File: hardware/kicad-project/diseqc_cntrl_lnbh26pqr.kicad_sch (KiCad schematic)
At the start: 22 parts, among them IC6 LNBH26PQR, J7 SMA_Sock, J8 SMA_Sock

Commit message: Add fiducials
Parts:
- C40: renamed from C36; footprint CAPC1608X90N -> Capacitor_SMD:C_0603_1608Metric
- renumbered C30 to C34, C31 to C35, C32 to C36, C33 to C37, C34 to C38, C35 to C39, D4 to D3, D5 to D4, D6 to D5, D7 to D6, R17 to R20, TP10 to TP11, TP11 to TP12

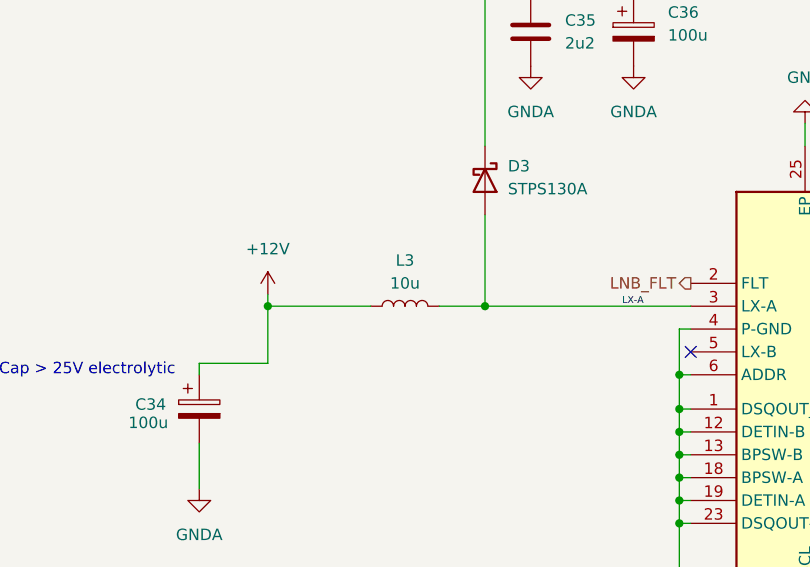
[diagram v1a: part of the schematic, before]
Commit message: Upgraded power supplies
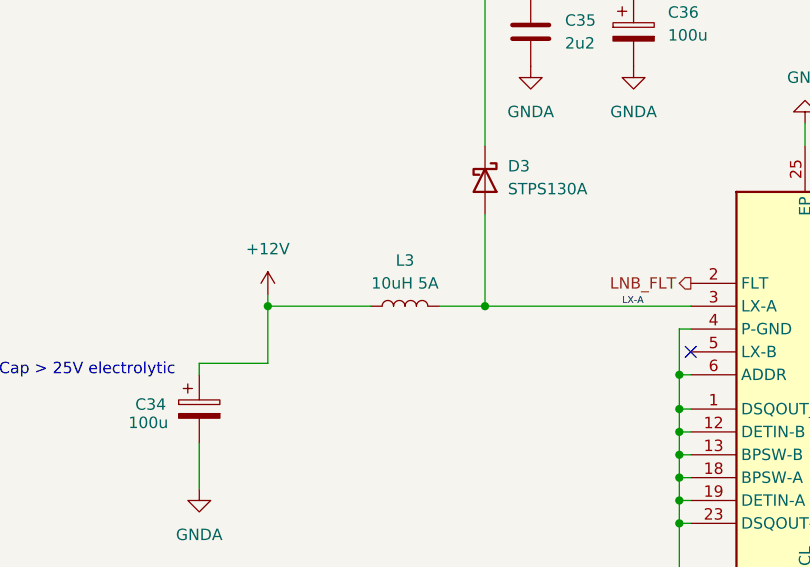
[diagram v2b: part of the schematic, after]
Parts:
- L3: value 10u -> 10uH 5A; footprint Inductor_SMD:L_0603_1608Metric -> ebnx_footprints:SRP6060FA4R7M; symbol diseqc_cntrl:L -> #InvenTree:L_10uH_5A_20%; InvenTree 97 -> 272; InvenTree Part L_10u_0603 -> (none); Mouser Part Number 963-CBMF1608T100K -> (none); Part URL (none) -> https://inventree.ebnx.net/web/part/272/
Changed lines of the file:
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@@
 	)
 	(symbol
-		(lib_id "diseqc_cntrl:L")
+		(lib_id "#InvenTree:L_10uH_5A_20%")
 		(at 88.9 87.63 90)
 		(unit 1)
@@
 			)
 		)
-		(property "Value" "10u"
+		(property "Value" "10uH 5A"
 			(at 88.9 85.09 90)
 			(show_name no)
@@
 			)
 		)
-		(property "Footprint" "Inductor_SMD:L_0603_1608Metric"
+		(property "Footprint" "ebnx_footprints:SRP6060FA4R7M"
 			(at 88.9 87.63 0)
 			(hide yes)
@@
 			)
 		)
-		(property "Mouser Part Number" "963-CBMF1608T100K"
+		(property "Mouser Part Number" ""
 			(at 88.9 87.63 90)
 			(hide yes)
@@
 			)
 		)
-		(property "InvenTree Part" "L_10u_0603"
+		(property "InvenTree Part" ""
 			(at 88.9 87.63 90)
 			(hide yes)
@@
 			)
 		)
-		(property "InvenTree" "97"
-			(at 88.9 87.63 90)
+		(property "InvenTree" "272"
+			(at 88.9 87.63 0)
 			(hide yes)
 			(show_name no)
@@
 				)
 			)
+		)
+		(property "Part URL" "https://inventree.ebnx.net/web/part/272/"
+			(at 88.9 87.63 0)
+			(hide yes)
+			(show_name no)
+			(do_not_autoplace no)
+			(effects
+				(font
+					(size 1.27 1.27)
+				)
+			)

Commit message: Corrected thermal/EMC issues
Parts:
- D4: footprint Diode_SMD:D_SMA-SMB_Universal_Handsoldering -> Diode_SMD:D_SMA
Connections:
- net GND: now also D6.1 (K1); no longer D6.3 (COMMON_ANODE)
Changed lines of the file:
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@@
 	)
 	(junction
-		(at 226.06 53.34)
-		(diameter 0)
-		(color 0 0 0 0)
-	)
-	(junction
 		(at 166.37 115.57)
 		(diameter 0)
@@
 	)
 	(no_connect
-		(at 120.65 92.71)
+		(at 226.06 34.29)
 	)
 	(no_connect
-		(at 190.5 34.29)
+		(at 120.65 92.71)
 	)
 	(no_connect
@@
 	(wire
 		(pts
+			(xy 190.5 34.29) (xy 185.42 34.29)
+		)
+		(stroke
+			(width 0)
+			(type default)
+		)
+	)
+	(wire
+		(pts
 			(xy 143.51 59.69) (xy 153.67 59.69)
 		)
@@
 	(wire
 		(pts
+			(xy 185.42 34.29) (xy 185.42 36.83)
+		)
+		(stroke
+			(width 0)
+			(type default)
+		)
+	)
+	(wire
+		(pts
 			(xy 195.58 67.31) (xy 199.39 67.31)
 		)
@@
 	(wire
 		(pts
-			(xy 226.06 34.29) (xy 226.06 53.34)
-		)
-		(stroke
-			(width 0)
-			(type default)
-		)
-	)
-	(wire
-		(pts
 			(xy 133.35 128.27) (xy 133.35 123.19)
 		)
@@
 			)
 		)
-		(property "Footprint" "Diode_SMD:D_SMA-SMB_Universal_Handsoldering"
+		(property "Footprint" "Diode_SMD:D_SMA"
 			(at 149.225 63.5 0)
 			(hide yes)
@@
 					(unit 1)
 				)
+			)
+		)
+	)
+	(symbol
+		(lib_id "power:GND")
+		(at 185.42 36.83 0)
+		(unit 1)
+		(body_style 1)
+		(exclude_from_sim no)
+		(in_bom yes)
+		(on_board yes)
+		(in_pos_files yes)
+		(dnp no)
+		(fields_autoplaced yes)
+		(property "Reference" "#PWR078"
+			(at 185.42 43.18 0)
+			(hide yes)
+			(show_name no)
+			(do_not_autoplace no)
+			(effects
+				(font
+					(size 1.27 1.27)
+				)
+			)
+		)
+		(property "Value" "GND"
+			(at 185.42 41.91 0)
+			(show_name no)
+			(do_not_autoplace no)
+			(effects
+				(font
+					(size 1.27 1.27)
+				)
+			)
+		)
+		(property "Footprint" ""
+			(at 185.42 36.83 0)
+			(hide yes)
+			(show_name no)
+			(do_not_autoplace no)
+			(effects
+				(font
+					(size 1.27 1.27)
+				)
+			)
+		)
+		(property "Datasheet" ""
+			(at 185.42 36.83 0)
+			(hide yes)
+			(show_name no)
+			(do_not_autoplace no)
+			(effects
+				(font
+					(size 1.27 1.27)
+				)
+			)
+		)
+		(property "Description" "Power symbol creates a global label with name \"GND\" , ground"
+			(at 185.42 36.83 0)
+			(hide yes)
+			(show_name no)
+			(do_not_autoplace no)
+			(effects
+				(font
+					(size 1.27 1.27)
+				)
+			)
+		)
+		(pin "1"
+		)
+		(instances
+			(project "diseqc_cntrl"
+				(path "/82a905d8-f1d7-4995-9c16-94cf3cdcaad9/65fcf1a0-d0f2-4bf0-9977-67dd9f84afa5/114baf94-7b4a-4d2d-92f4-f2fc3fb70423"
+					(reference "#PWR078")
+					(unit 1)
+				)

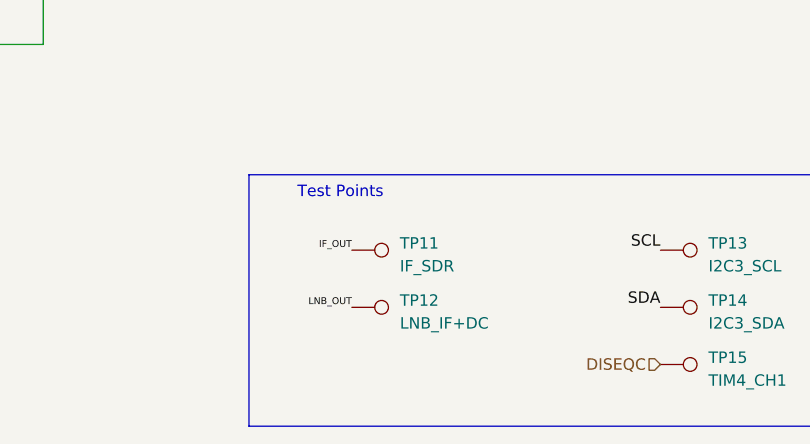
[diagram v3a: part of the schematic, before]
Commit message: Removed unnecessary test points
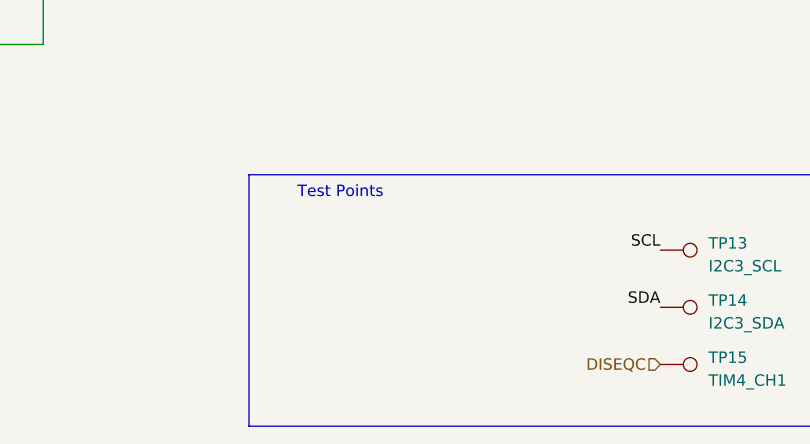
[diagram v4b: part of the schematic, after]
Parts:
- removed TP11: IF_SDR, ebnx_footprints:TestPoint_THTPad_D1.0mm_Drill0.5mm_annotated, symbol ebnx_symbols:TestPoint_Annotated_Silkscreen
- removed TP12: LNB_IF+DC, ebnx_footprints:TestPoint_THTPad_D1.0mm_Drill0.5mm_annotated, symbol ebnx_symbols:TestPoint_Annotated_Silkscreen

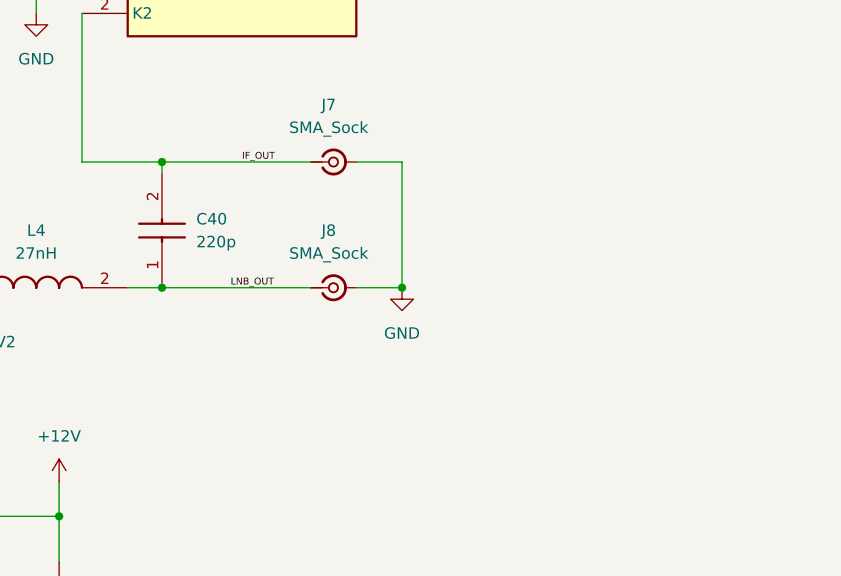
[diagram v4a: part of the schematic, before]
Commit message: RF impedance matching
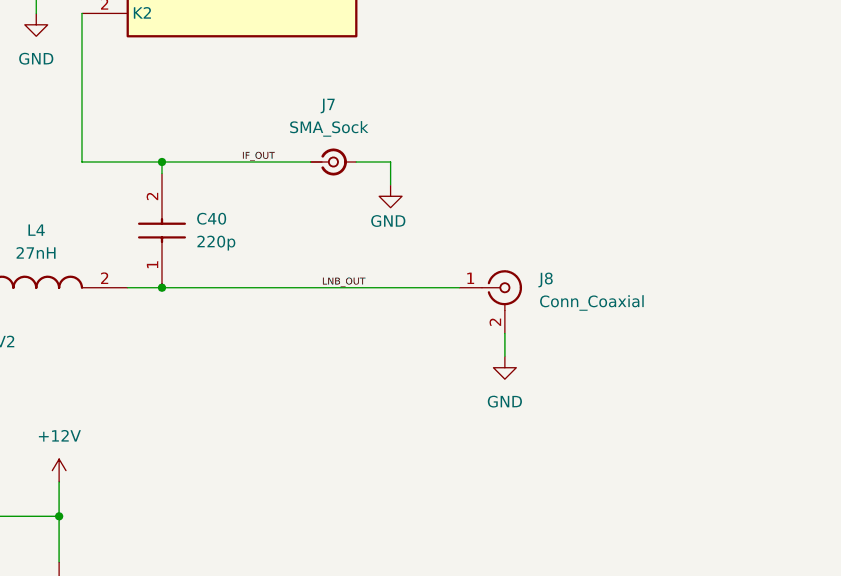
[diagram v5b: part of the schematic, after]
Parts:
- J8: value SMA_Sock -> Conn_Coaxial; footprint Connector_Coaxial:SMA_Molex_73251-1153_EdgeMount_Horizontal -> ebnx_footprints:AMPHENOL_531-40156; symbol diseqc_cntrl:Conn_Coaxial_Small -> Connector:Conn_Coaxial; Height (none) -> (none); InvenTree 81 -> 277; InvenTree Part J_RF_SMA_SKT -> (none); MPN (none) -> 531-40156; Manufacturer_Name (none) -> Amphenol; Manufacturer_Part_Number (none) -> 531-40156; Maufacturer_Part_Number (none) -> 531-40156; Mouser Part Number 538-73251-1153 -> 523-531-40156; Mouser Price/Stock (none) -> https://www.mouser.co.uk/ProductDetail/Amphenol-RF/531-40156; Part URL (none) -> https://inventree.ebnx.net/web/part/277/
